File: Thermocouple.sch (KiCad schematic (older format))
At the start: 22 parts, among them P2 CONN_3X2, P3 CONN_2, U2 MCP3901, U3 LMT84, U4 OPA4170

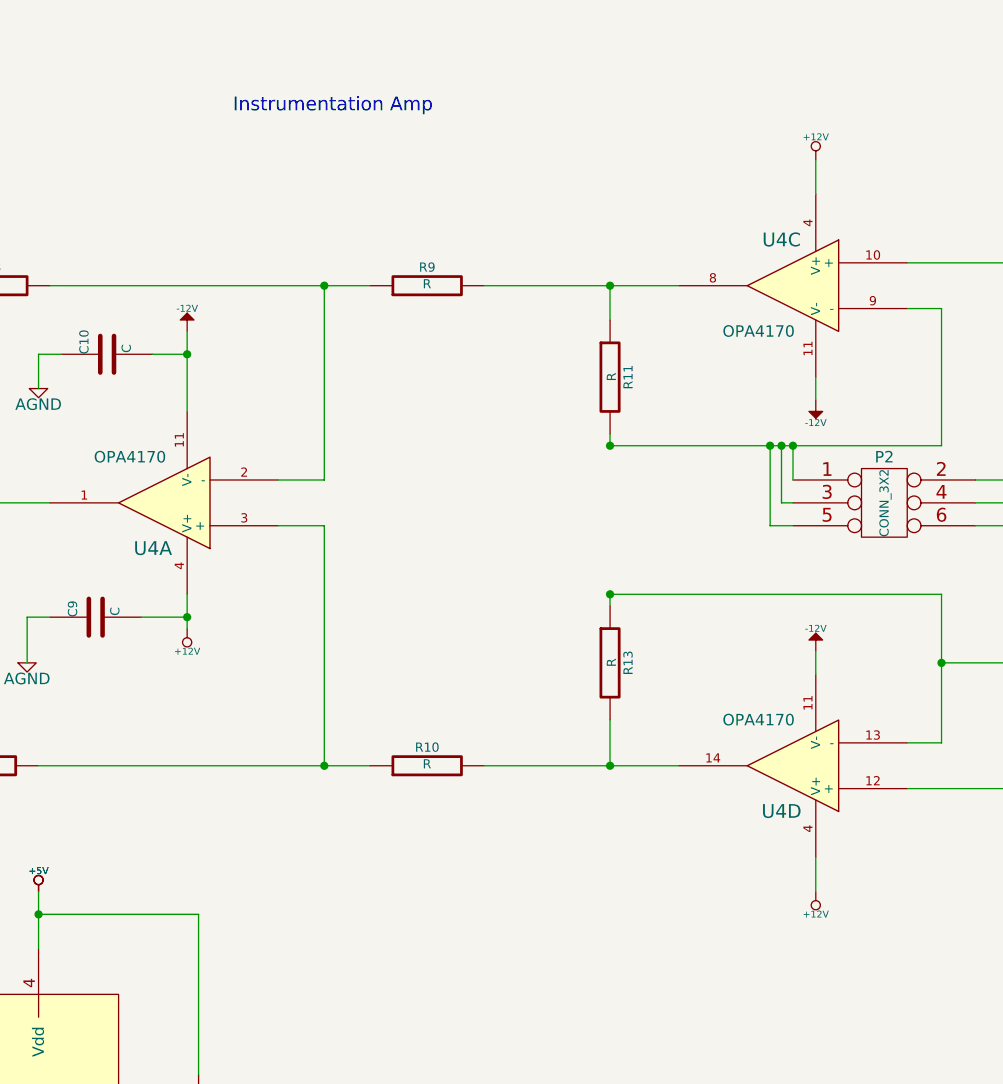
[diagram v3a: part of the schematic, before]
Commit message: Added Ground Planes, Heatsinks, Moved components
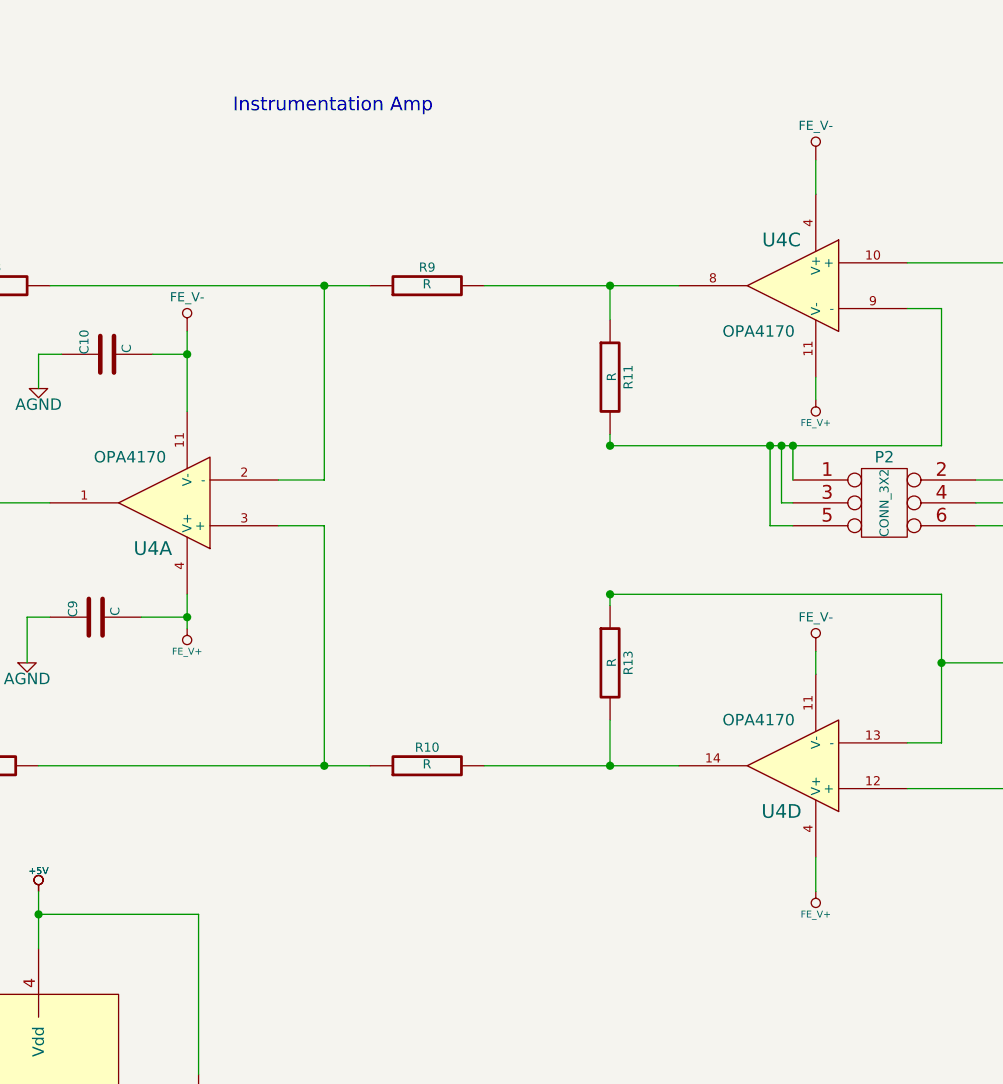
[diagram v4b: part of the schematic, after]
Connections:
- net +12V renamed FE_V+
- net FE_V+: now also U4.11 (V-); no longer U4.4 (V+)
- net -12V renamed FE_V-
- net FE_V-: now also U4.4 (V+); no longer U4.11 (V-)
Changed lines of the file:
@@
-EESchema Schematic File Version 2  date 10/22/2013 9:09:24 PM
+EESchema Schematic File Version 2  date 10/27/2013 11:25:35 PM
 LIBS:power
 LIBS:device
@@
 Sheet 2 9
 Title ""
-Date "23 oct 2013"
+Date "28 oct 2013"
 Rev ""
 Comp ""
@@
 	0    -1   -1   0
 $EndComp
-$Comp
-L -12V #PWR01
-U 1 1 523646A5
-P 6250 2550
-F 0 "#PWR01" H 6250 2680 20  0001 C CNN
-F 1 "-12V" H 6250 2650 30  0000 C CNN
-F 2 "" H 6250 2550 60  0000 C CNN
-F 3 "" H 6250 2550 60  0000 C CNN
-	1    6250 2550
-	1    0    0    -1
-$EndComp
-$Comp
-L -12V #PWR02
-U 1 1 523646B2
-P 9000 2850
-F 0 "#PWR02" H 9000 2980 20  0001 C CNN
-F 1 "-12V" H 9000 2950 30  0000 C CNN
-F 2 "" H 9000 2850 60  0000 C CNN
-F 3 "" H 9000 2850 60  0000 C CNN
-	1    9000 2850
-	-1   0    0    1
-$EndComp
-$Comp
-L -12V #PWR03
-U 1 1 523646B8
-P 9000 3950
-F 0 "#PWR03" H 9000 4080 20  0001 C CNN
-F 1 "-12V" H 9000 4050 30  0000 C CNN
-F 2 "" H 9000 3950 60  0000 C CNN
-F 3 "" H 9000 3950 60  0000 C CNN
-	1    9000 3950
-	1    0    0    -1
-$EndComp
-$Comp
-L +12V #PWR04
-U 1 1 5236471D
-P 6250 3850
-F 0 "#PWR04" H 6250 3800 20  0001 C CNN
-F 1 "+12V" H 6250 3950 30  0000 C CNN
-F 2 "" H 6250 3850 60  0000 C CNN
-F 3 "" H 6250 3850 60  0000 C CNN
-	1    6250 3850
-	-1   0    0    1
-$EndComp
-$Comp
-L +12V #PWR05
-U 1 1 5236474B
-P 9000 1800
-F 0 "#PWR05" H 9000 1750 20  0001 C CNN
-F 1 "+12V" H 9000 1900 30  0000 C CNN
-F 2 "" H 9000 1800 60  0000 C CNN
-F 3 "" H 9000 1800 60  0000 C CNN
-	1    9000 1800
-	1    0    0    -1
-$EndComp
-$Comp
-L +12V #PWR06
-U 1 1 52364796
-P 9000 5000
-F 0 "#PWR06" H 9000 4950 20  0001 C CNN
-F 1 "+12V" H 9000 5100 30  0000 C CNN
-F 2 "" H 9000 5000 60  0000 C CNN
-F 3 "" H 9000 5000 60  0000 C CNN
-	1    9000 5000
-	-1   0    0    1
-$EndComp
 Wire Wire Line
 	7550 2350 8400 2350
@@
 	9000 5000 9000 4850
 $Comp
-L AGND #PWR07
+L AGND #PWR01
 U 1 1 52364808
 P 4900 4700
-F 0 "#PWR07" H 4900 4700 40  0001 C CNN
+F 0 "#PWR01" H 4900 4700 40  0001 C CNN
 F 1 "AGND" H 4900 4630 50  0000 C CNN
 F 2 "" H 4900 4700 60  0000 C CNN
@@
 Connection ~ 5600 6800
 $Comp
-L AGND #PWR08
+L AGND #PWR02
 U 1 1 525797B7
 P 4800 6900
-F 0 "#PWR08" H 4800 6900 40  0001 C CNN
+F 0 "#PWR02" H 4800 6900 40  0001 C CNN
 F 1 "AGND" H 4800 6830 50  0000 C CNN
 F 2 "" H 4800 6900 60  0000 C CNN
@@
 Connection ~ 4800 6800
 $Comp
-L +5V #PWR09
+L +5V #PWR03
 U 1 1 5257A1D1
 P 5600 5000
-F 0 "#PWR09" H 5600 5090 20  0001 C CNN
+F 0 "#PWR03" H 5600 5090 20  0001 C CNN
 F 1 "+5V" H 5600 5090 30  0000 C CNN
 F 2 "~" H 5600 5000 60  0000 C CNN
@@
 Connection ~ 6250 3800
 $Comp
-L AGND #PWR010
+L AGND #PWR04
 U 1 1 5257A2EE
 P 5550 4000
-F 0 "#PWR010" H 5550 4000 40  0001 C CNN
+F 0 "#PWR04" H 5550 4000 40  0001 C CNN
 F 1 "AGND" H 5550 3930 50  0000 C CNN
 F 2 "" H 5550 4000 60  0000 C CNN
@@
 $EndComp
 $Comp
-L AGND #PWR011
+L AGND #PWR05
 U 1 1 5257A35E
 P 5600 2800
-F 0 "#PWR011" H 5600 2800 40  0001 C CNN
+F 0 "#PWR05" H 5600 2800 40  0001 C CNN
 F 1 "AGND" H 5600 2730 50  0000 C CNN
 F 2 "" H 5600 2800 60  0000 C CNN
@@
 	6050 3800 6250 3800
 $Comp
-L +5V #PWR012
+L +5V #PWR06
 U 1 1 5257A5A4
 P 5600 5000
-F 0 "#PWR012" H 5600 5090 20  0001 C CNN
+F 0 "#PWR06" H 5600 5090 20  0001 C CNN
 F 1 "+5V" H 5600 5090 30  0000 C CNN
 F 2 "~" H 5600 5000 60  0000 C CNN
@@
 $EndComp
 $Comp
-L +5V #PWR013
+L +5V #PWR07
 U 1 1 5257A5AA
 P 3100 1300
-F 0 "#PWR013" H 3100 1390 20  0001 C CNN
+F 0 "#PWR07" H 3100 1390 20  0001 C CNN
 F 1 "+5V" H 3100 1390 30  0000 C CNN
 F 2 "~" H 3100 1300 60  0000 C CNN
@@
 Connection ~ 3100 1500
 $Comp
-L AGND #PWR014
+L AGND #PWR08
 U 1 1 5257A818
 P 3700 1600
-F 0 "#PWR014" H 3700 1600 40  0001 C CNN
+F 0 "#PWR08" H 3700 1600 40  0001 C CNN
 F 1 "AGND" H 3700 1530 50  0000 C CNN
 F 2 "" H 3700 1600 60  0000 C CNN
@@
 Connection ~ 2400 1550
 $Comp
-L AGND #PWR015
+L AGND #PWR09
 U 1 1 5257A963
 P 1750 1650
-F 0 "#PWR015" H 1750 1650 40  0001 C CNN
+F 0 "#PWR09" H 1750 1650 40  0001 C CNN
 F 1 "AGND" H 1750 1580 50  0000 C CNN
 F 2 "" H 1750 1650 60  0000 C CNN
@@
 	1750 1550 1900 1550
 $Comp
-L AGND #PWR016
+L AGND #PWR010
 U 1 1 5257A9D6
 P 2300 4850
-F 0 "#PWR016" H 2300 4850 40  0001 C CNN
+F 0 "#PWR010" H 2300 4850 40  0001 C CNN
 F 1 "AGND" H 2300 4780 50  0000 C CNN
 F 2 "" H 2300 4850 60  0000 C CNN
@@
 	3100 4600 3100 4850
 $Comp
-L AGND #PWR017
+L AGND #PWR011
 U 1 1 5257AABC
 P 3100 4850
-F 0 "#PWR017" H 3100 4850 40  0001 C CNN
+F 0 "#PWR011" H 3100 4850 40  0001 C CNN
 F 1 "AGND" H 3100 4780 50  0000 C CNN
 F 2 "" H 3100 4850 60  0000 C CNN
@@
 $EndComp
 $Comp
-L +5V #PWR018
+L +5V #PWR012
 U 1 1 5257AAC2
 P 2400 1300
-F 0 "#PWR018" H 2400 1390 20  0001 C CNN
+F 0 "#PWR012" H 2400 1390 20  0001 C CNN
 F 1 "+5V" H 2400 1390 30  0000 C CNN
 F 2 "~" H 2400 1300 60  0000 C CNN
@@
 Wire Wire Line
 	4550 3900 4550 6050
+$Comp
+L FE_V- #PWR13
+U 1 1 526E01DB
+P 6250 2550
+F 0 "#PWR13" H 6250 2750 40  0001 C CNN
+F 1 "FE_V-" H 6250 2700 40  0000 C CNN
+F 2 "~" H 6250 2550 60  0000 C CNN
+F 3 "~" H 6250 2550 60  0000 C CNN
+	1    6250 2550
+	1    0    0    -1
+$EndComp
+$Comp
+L FE_V+ #PWR013
+U 1 1 526E01E1
+P 6250 3850
+F 0 "#PWR013" H 6250 3950 30  0001 C CNN
+F 1 "FE_V+" H 6250 3950 30  0000 C CNN
+F 2 "~" H 6250 3850 60  0000 C CNN
+F 3 "~" H 6250 3850 60  0000 C CNN
+	1    6250 3850
+	-1   0    0    1
+$EndComp
+$Comp
+L FE_V+ #PWR014
+U 1 1 526E01F1
+P 9000 5000
+F 0 "#PWR014" H 9000 5100 30  0001 C CNN
+F 1 "FE_V+" H 9000 5100 30  0000 C CNN
+F 2 "~" H 9000 5000 60  0000 C CNN
+F 3 "~" H 9000 5000 60  0000 C CNN
+	1    9000 5000
+	-1   0    0    1
+$EndComp
+$Comp
+L FE_V- #PWR17
+U 1 1 526E0201
+P 9000 3950
+F 0 "#PWR17" H 9000 4150 40  0001 C CNN
+F 1 "FE_V-" H 9000 4100 40  0000 C CNN
+F 2 "~" H 9000 3950 60  0000 C CNN
+F 3 "~" H 9000 3950 60  0000 C CNN
+	1    9000 3950
+	1    0    0    -1
+$EndComp
+$Comp
+L FE_V- #PWR15
+U 1 1 526E0207
+P 9000 1800
+F 0 "#PWR15" H 9000 2000 40  0001 C CNN
+F 1 "FE_V-" H 9000 1950 40  0000 C CNN
+F 2 "~" H 9000 1800 60  0000 C CNN
+F 3 "~" H 9000 1800 60  0000 C CNN
+	1    9000 1800
+	1    0    0    -1
+$EndComp
+$Comp
+L FE_V+ #PWR015
+U 1 1 526E020D
+P 9000 2850
+F 0 "#PWR015" H 9000 2950 30  0001 C CNN
+F 1 "FE_V+" H 9000 2950 30  0000 C CNN
+F 2 "~" H 9000 2850 60  0000 C CNN
+F 3 "~" H 9000 2850 60  0000 C CNN
+	1    9000 2850
+	-1   0    0    1
+$EndComp
 $EndSCHEMATC

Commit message: Layout Work Session 4 Output
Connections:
- net AGND renamed GND_TC
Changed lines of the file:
@@
-EESchema Schematic File Version 2  date 11/2/2013 7:04:39 PM
+EESchema Schematic File Version 2  date 11/7/2013 10:50:27 PM
 LIBS:power
 LIBS:device
@@
 Sheet 2 9
 Title ""
-Date "2 nov 2013"
+Date "8 nov 2013"
 Rev ""
 Comp ""
@@
 Wire Wire Line
 	9000 5000 9000 4850
-$Comp
-L AGND #PWR8
-U 1 1 52364808
-P 4900 4700
-F 0 "#PWR8" H 4900 4700 40  0001 C CNN
-F 1 "AGND" H 4900 4630 50  0000 C CNN
-F 2 "" H 4900 4700 60  0000 C CNN
-F 3 "" H 4900 4700 60  0000 C CNN
-	1    4900 4700
-	1    0    0    -1
-$EndComp
 Wire Wire Line
 	4900 4450 5100 4450
@@
 	5700 6800 5700 6650
 Connection ~ 5600 6800
-$Comp
-L AGND #PWR7
-U 1 1 525797B7
-P 4800 6900
-F 0 "#PWR7" H 4800 6900 40  0001 C CNN
-F 1 "AGND" H 4800 6830 50  0000 C CNN
-F 2 "" H 4800 6900 60  0000 C CNN
-F 3 "" H 4800 6900 60  0000 C CNN
-	1    4800 6900
-	1    0    0    -1
-$EndComp
 Wire Wire Line
 	4800 6900 4800 6800
 Connection ~ 4800 6800
 $Comp
-L +5V #PWR11
+L +5V #PWR03
 U 1 1 5257A1D1
 P 5600 5000
-F 0 "#PWR11" H 5600 5090 20  0001 C CNN
+F 0 "#PWR03" H 5600 5090 20  0001 C CNN
 F 1 "+5V" H 5600 5090 30  0000 C CNN
 F 2 "~" H 5600 5000 60  0000 C CNN
@@
 Connection ~ 6250 3800
 $Comp
-L AGND #PWR9
-U 1 1 5257A2EE
-P 5550 4000
-F 0 "#PWR9" H 5550 4000 40  0001 C CNN
-F 1 "AGND" H 5550 3930 50  0000 C CNN
-F 2 "" H 5550 4000 60  0000 C CNN
-F 3 "" H 5550 4000 60  0000 C CNN
-	1    5550 4000
-	1    0    0    -1
-$EndComp
-$Comp
 L C C10
 U 1 1 5257A357
@@
 	0    -1   -1   0
 $EndComp
-$Comp
-L AGND #PWR10
-U 1 1 5257A35E
-P 5600 2800
-F 0 "#PWR10" H 5600 2800 40  0001 C CNN
-F 1 "AGND" H 5600 2730 50  0000 C CNN
-F 2 "" H 5600 2800 60  0000 C CNN
-F 3 "" H 5600 2800 60  0000 C CNN
-	1    5600 2800
-	1    0    0    -1
-$EndComp
 Wire Wire Line
 	6100 2650 6250 2650
@@
 	6050 3800 6250 3800
 $Comp
-L +5V #PWR12
+L +5V #PWR06
 U 1 1 5257A5A4
 P 5600 5000
-F 0 "#PWR12" H 5600 5090 20  0001 C CNN
+F 0 "#PWR06" H 5600 5090 20  0001 C CNN
 F 1 "+5V" H 5600 5090 30  0000 C CNN
 F 2 "~" H 5600 5000 60  0000 C CNN
@@
 $EndComp
 $Comp
-L +5V #PWR4
+L +5V #PWR07
 U 1 1 5257A5AA
 P 3100 1300
-F 0 "#PWR4" H 3100 1390 20  0001 C CNN
+F 0 "#PWR07" H 3100 1390 20  0001 C CNN
 F 1 "+5V" H 3100 1390 30  0000 C CNN
 F 2 "~" H 3100 1300 60  0000 C CNN
@@
 	3100 1500 3200 1500
 Connection ~ 3100 1500
-$Comp
-L AGND #PWR6
-U 1 1 5257A818
-P 3700 1600
-F 0 "#PWR6" H 3700 1600 40  0001 C CNN
-F 1 "AGND" H 3700 1530 50  0000 C CNN
-F 2 "" H 3700 1600 60  0000 C CNN
-F 3 "" H 3700 1600 60  0000 C CNN
-	1    3700 1600
-	1    0    0    -1
-$EndComp
 Wire Wire Line
 	3700 1600 3700 1500
@@
 	2400 1550 2300 1550
 Connection ~ 2400 1550
-$Comp
-L AGND #PWR1
-U 1 1 5257A963
-P 1750 1650
-F 0 "#PWR1" H 1750 1650 40  0001 C CNN
-F 1 "AGND" H 1750 1580 50  0000 C CNN
-F 2 "" H 1750 1650 60  0000 C CNN
-F 3 "" H 1750 1650 60  0000 C CNN
-	1    1750 1650
-	1    0    0    -1
-$EndComp
 Wire Wire Line
 	1750 1650 1750 1550
 Wire Wire Line
 	1750 1550 1900 1550
-$Comp
-L AGND #PWR2
-U 1 1 5257A9D6
-P 2300 4850
-F 0 "#PWR2" H 2300 4850 40  0001 C CNN
-F 1 "AGND" H 2300 4780 50  0000 C CNN
-F 2 "" H 2300 4850 60  0000 C CNN
-F 3 "" H 2300 4850 60  0000 C CNN
-	1    2300 4850
-	1    0    0    -1
-$EndComp
 Wire Wire Line
 	2300 4850 2300 4600
@@
 	3100 4600 3100 4850
 $Comp
-L AGND #PWR5
-U 1 1 5257AABC
-P 3100 4850
-F 0 "#PWR5" H 3100 4850 40  0001 C CNN
-F 1 "AGND" H 3100 4780 50  0000 C CNN
-F 2 "" H 3100 4850 60  0000 C CNN
-F 3 "" H 3100 4850 60  0000 C CNN
-	1    3100 4850
-	1    0    0    -1
-$EndComp
-$Comp
-L +5V #PWR3
+L +5V #PWR012
 U 1 1 5257AAC2
 P 2400 1300
-F 0 "#PWR3" H 2400 1390 20  0001 C CNN
+F 0 "#PWR012" H 2400 1390 20  0001 C CNN
 F 1 "+5V" H 2400 1390 30  0000 C CNN
 F 2 "~" H 2400 1300 60  0000 C CNN
@@
 $EndComp
 $Comp
-L FE_V+ #PWR14
+L FE_V+ #PWR013
 U 1 1 526E01E1
 P 6250 3850
-F 0 "#PWR14" H 6250 3950 30  0001 C CNN
+F 0 "#PWR013" H 6250 3950 30  0001 C CNN
 F 1 "FE_V+" H 6250 3950 30  0000 C CNN
 F 2 "~" H 6250 3850 60  0000 C CNN
@@
 $EndComp
 $Comp
-L FE_V+ #PWR18
+L FE_V+ #PWR014
 U 1 1 526E01F1
 P 9000 5000
-F 0 "#PWR18" H 9000 5100 30  0001 C CNN
+F 0 "#PWR014" H 9000 5100 30  0001 C CNN
 F 1 "FE_V+" H 9000 5100 30  0000 C CNN
 F 2 "~" H 9000 5000 60  0000 C CNN
@@
 $EndComp
 $Comp
-L FE_V+ #PWR16
+L FE_V+ #PWR015
 U 1 1 526E020D
 P 9000 2850
-F 0 "#PWR16" H 9000 2950 30  0001 C CNN
+F 0 "#PWR015" H 9000 2950 30  0001 C CNN
 F 1 "FE_V+" H 9000 2950 30  0000 C CNN
 F 2 "~" H 9000 2850 60  0000 C CNN
@@
 	-1   0    0    1
 $EndComp
+$Comp
+L GND_TC #PWR?
+U 1 1 527CE7CA
+P 4800 6900
+F 0 "#PWR?" H 4800 6900 30  0001 C CNN
+F 1 "GND_TC" H 4800 6830 30  0000 C CNN
+F 2 "~" H 4800 6900 60  0000 C CNN
+F 3 "~" H 4800 6900 60  0000 C CNN
+	1    4800 6900
+	1    0    0    -1
+$EndComp
+$Comp
+L GND_TC #PWR?
+U 1 1 527CE7D0
+P 3100 4850
+F 0 "#PWR?" H 3100 4850 30  0001 C CNN
+F 1 "GND_TC" H 3100 4780 30  0000 C CNN
+F 2 "~" H 3100 4850 60  0000 C CNN
+F 3 "~" H 3100 4850 60  0000 C CNN
+	1    3100 4850
+	1    0    0    -1
+$EndComp
+$Comp
+L GND_TC #PWR?
+U 1 1 527CE7D6
+P 2300 4850
+F 0 "#PWR?" H 2300 4850 30  0001 C CNN
+F 1 "GND_TC" H 2300 4780 30  0000 C CNN
+F 2 "~" H 2300 4850 60  0000 C CNN
+F 3 "~" H 2300 4850 60  0000 C CNN
+	1    2300 4850
+	1    0    0    -1
+$EndComp
+$Comp
+L GND_TC #PWR?
+U 1 1 527CE7DC
+P 1750 1650
+F 0 "#PWR?" H 1750 1650 30  0001 C CNN
+F 1 "GND_TC" H 1750 1580 30  0000 C CNN
+F 2 "~" H 1750 1650 60  0000 C CNN
+F 3 "~" H 1750 1650 60  0000 C CNN
+	1    1750 1650
+	1    0    0    -1
+$EndComp
+$Comp
+L GND_TC #PWR?
+U 1 1 527CE7E2
+P 3700 1600
+F 0 "#PWR?" H 3700 1600 30  0001 C CNN
+F 1 "GND_TC" H 3700 1530 30  0000 C CNN
+F 2 "~" H 3700 1600 60  0000 C CNN
+F 3 "~" H 3700 1600 60  0000 C CNN
+	1    3700 1600
+	1    0    0    -1
+$EndComp
+$Comp
+L GND_TC #PWR?
+U 1 1 527CE7E8
+P 5600 2800
+F 0 "#PWR?" H 5600 2800 30  0001 C CNN
+F 1 "GND_TC" H 5600 2730 30  0000 C CNN
+F 2 "~" H 5600 2800 60  0000 C CNN
+F 3 "~" H 5600 2800 60  0000 C CNN
+	1    5600 2800
+	1    0    0    -1
+$EndComp
+$Comp
+L GND_TC #PWR?
+U 1 1 527CE7EE
+P 5550 4000
+F 0 "#PWR?" H 5550 4000 30  0001 C CNN
+F 1 "GND_TC" H 5550 3930 30  0000 C CNN
+F 2 "~" H 5550 4000 60  0000 C CNN
+F 3 "~" H 5550 4000 60  0000 C CNN
+	1    5550 4000
+	1    0    0    -1
+$EndComp
+$Comp
+L GND_TC #PWR?
+U 1 1 527CE7F4
+P 4900 4700
+F 0 "#PWR?" H 4900 4700 30  0001 C CNN
+F 1 "GND_TC" H 4900 4630 30  0000 C CNN
+F 2 "~" H 4900 4700 60  0000 C CNN
+F 3 "~" H 4900 4700 60  0000 C CNN
+	1    4900 4700
+	1    0    0    -1
+$EndComp
 $EndSCHEMATC
